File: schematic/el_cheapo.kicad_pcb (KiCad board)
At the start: 2 copper layers, 100.7 x 80.4 mm, 57 parts, among them J1 Conn_01x02, J2 Conn_01x02, J3 Conn_01x02, Q1 TIP32A, Q2 2N3904, Q3 2N3906, Q4 2N3904, Q5 TIP31A, Q6 TIP32A, Q7 2N3055, Q8 2N3055

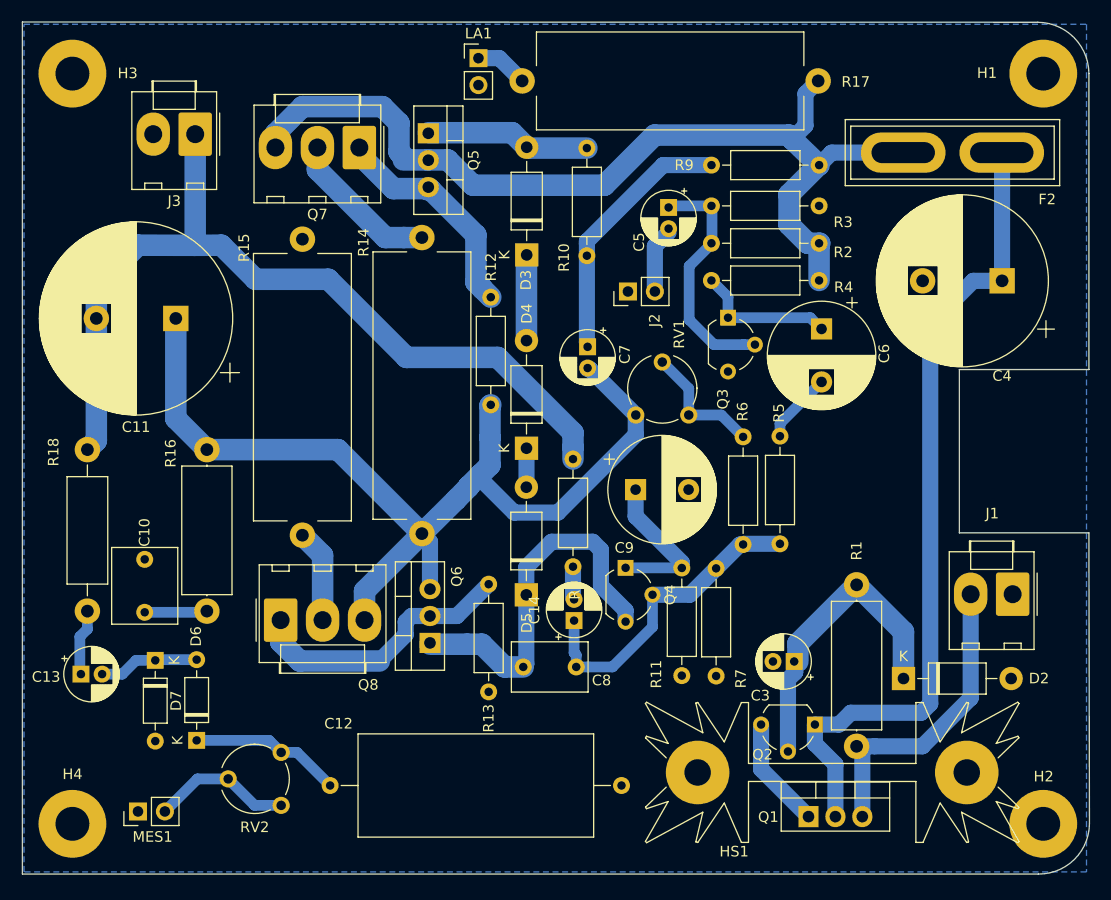
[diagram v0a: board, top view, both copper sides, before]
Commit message: first decent version of dual channel opamp version.
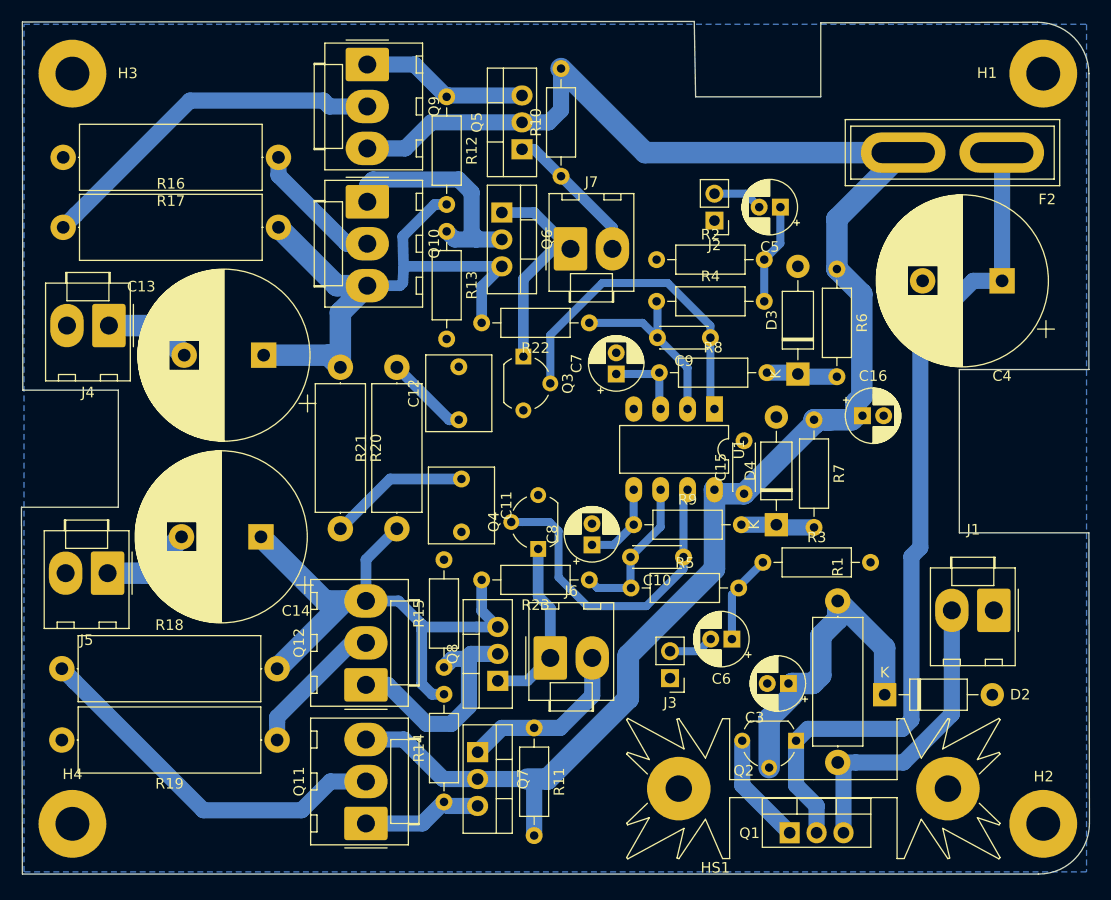
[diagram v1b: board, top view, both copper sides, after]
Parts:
- removed D5: 1N4001, Diode_THT:D_DO-41_SOD81_P10.16mm_Horizontal
- removed D6, D7: 1N914, Diode_THT:D_DO-35_SOD27_P7.62mm_Horizontal
- removed LA1: Lamp, Connector_PinHeader_2.54mm:PinHeader_1x02_P2.54mm_Vertical
- removed MES1: Amperemeter_DC, Connector_PinHeader_2.54mm:PinHeader_1x02_P2.54mm_Vertical
- removed RV1: 120k, Potentiometer_THT:Potentiometer_Piher_PT-6-V_Vertical
- removed RV2: 1k_100K, Potentiometer_THT:Potentiometer_Piher_PT-6-V_Vertical
- added C15: 0.1uF, Capacitor_THT:C_Disc_D4.3mm_W1.9mm_P5.00mm, F.Cu at (155.7, 102.6)
- added C16: 10uF, Capacitor_THT:CP_Radial_D5.0mm_P2.00mm, F.Cu at (166.9, 95.2)
- added J4: Conn_01x02, Connector_Molex:Molex_KK-396_A-41791-0002_1x02_P3.96mm_Vertical, F.Cu at (95.8, 86.7)
- added J5: Conn_01x02, Connector_Molex:Molex_KK-396_A-41791-0002_1x02_P3.96mm_Vertical, F.Cu at (95.6, 110.1)
- added J6: Conn_01x02, Connector_Molex:Molex_KK-396_A-41791-0002_1x02_P3.96mm_Vertical, F.Cu at (137.4, 118.1)
- added J7: Conn_01x02, Connector_Molex:Molex_KK-396_A-41791-0002_1x02_P3.96mm_Vertical, F.Cu at (139.3, 79.5)
- added Q10: 2N3055, Connector_Molex:Molex_KK-396_A-41791-0003_1x03_P3.96mm_Vertical, F.Cu at (120.1, 75.1)
- added Q11: 2N3055, Connector_Molex:Molex_KK-396_A-41791-0003_1x03_P3.96mm_Vertical, F.Cu at (120.0, 133.7)
- added Q12: 2N3055, Connector_Molex:Molex_KK-396_A-41791-0003_1x03_P3.96mm_Vertical, F.Cu at (120.0, 120.7)
- added Q9: 2N3055, Connector_Molex:Molex_KK-396_A-41791-0003_1x03_P3.96mm_Vertical, F.Cu at (120.1, 62.1)
- added R19: 0R47 1W, Resistor_THT:R_Axial_DIN0617_L17.0mm_D6.0mm_P20.32mm_Horizontal, F.Cu at (111.6, 125.9)
- added R20: 18R 1W, Resistor_THT:R_Axial_DIN0414_L11.9mm_D4.5mm_P15.24mm_Horizontal, F.Cu at (117.6, 90.7)
- added R21: 18R 1W, Resistor_THT:R_Axial_DIN0414_L11.9mm_D4.5mm_P15.24mm_Horizontal, F.Cu at (122.9, 105.9)
- added R22: 100K, Resistor_THT:R_Axial_DIN0207_L6.3mm_D2.5mm_P10.16mm_Horizontal, F.Cu at (141.1, 86.5)
- added R23: 100K, Resistor_THT:R_Axial_DIN0207_L6.3mm_D2.5mm_P10.16mm_Horizontal, F.Cu at (141.1, 110.7)
- added U1: NE5532, Package_DIP:DIP-8_W7.62mm_LongPads, F.Cu at (152.9, 94.6)
- C10: value 100nF -> 22pF; footprint Capacitor_THT:C_Rect_L7.0mm_W6.0mm_P5.00mm -> Capacitor_THT:C_Disc_D4.3mm_W1.9mm_P5.00mm
- C11: value 2200uF -> 100nF; footprint Capacitor_THT:CP_Radial_D18.0mm_P7.50mm -> Capacitor_THT:C_Rect_L7.0mm_W6.0mm_P5.00mm
- C12: value 0.1uF -> 100nF; footprint Capacitor_THT:C_Axial_L22.0mm_D9.5mm_P27.50mm_Horizontal -> Capacitor_THT:C_Rect_L7.0mm_W6.0mm_P5.00mm
- C13: value 10uF -> 2200uF; footprint Capacitor_THT:CP_Radial_D5.0mm_P2.00mm -> Capacitor_THT:CP_Radial_D16.0mm_P7.50mm
- C14: value 47uF -> 2200uF; footprint Capacitor_THT:CP_Radial_D5.0mm_P2.00mm -> Capacitor_THT:CP_Radial_D16.0mm_P7.50mm
- C6: value 220uF -> 10uF; footprint Capacitor_THT:CP_Radial_D10.0mm_P5.00mm -> Capacitor_THT:CP_Radial_D5.0mm_P2.00mm
- C7: value 22uF -> 10uF
- C8: value 100pF -> 10uF; footprint Capacitor_THT:C_Rect_L7.0mm_W4.5mm_P5.00mm -> Capacitor_THT:CP_Radial_D5.0mm_P2.00mm
- C9: value 220uF -> 22pF; footprint Capacitor_THT:CP_Radial_D10.0mm_P5.00mm -> Capacitor_THT:C_Disc_D4.3mm_W1.9mm_P5.00mm
- D2: value 33 -> 39V
- D3, D4: value 1N4001 -> 1N47xxA
- F2: value 1A -> 2A
- J3: footprint Connector_Molex:Molex_KK-396_A-41791-0002_1x02_P3.96mm_Vertical -> Connector_PinHeader_2.54mm:PinHeader_1x02_P2.54mm_Vertical
- Q4: value 2N3904 -> 2N3906
- Q7: value 2N3055 -> TIP31A; footprint Connector_Molex:Molex_KK-396_A-41791-0003_1x03_P3.96mm_Vertical -> Package_TO_SOT_THT:TO-220-3_Vertical
- Q8: value 2N3055 -> TIP32A; footprint Connector_Molex:Molex_KK-396_A-41791-0003_1x03_P3.96mm_Vertical -> Package_TO_SOT_THT:TO-220-3_Vertical
- R10: value 3K3 -> 1k
- R11: value 330R -> 1K
- R14, R15: value 0R47 1W -> 270; footprint Resistor_THT:R_Axial_Power_L25.0mm_W9.0mm_P27.94mm -> Resistor_THT:R_Axial_DIN0207_L6.3mm_D2.5mm_P10.16mm_Horizontal
- R16: value 18R 1W -> 0R47 1W; footprint Resistor_THT:R_Axial_DIN0414_L11.9mm_D4.5mm_P15.24mm_Horizontal -> Resistor_THT:R_Axial_DIN0617_L17.0mm_D6.0mm_P20.32mm_Horizontal
- R17: value 470R 2W -> 0R47 1W; footprint Resistor_THT:R_Axial_Power_L25.0mm_W9.0mm_P27.94mm -> Resistor_THT:R_Axial_DIN0617_L17.0mm_D6.0mm_P20.32mm_Horizontal
- R18: value 1k_100k 1W -> 0R47 1W; footprint Resistor_THT:R_Axial_DIN0411_L9.9mm_D3.6mm_P15.24mm_Horizontal -> Resistor_THT:R_Axial_DIN0617_L17.0mm_D6.0mm_P20.32mm_Horizontal
- R2, R3: value 220k -> 100k
- R4: value 10k -> 12k
- R5: value 1k -> 12k
- R6: value 22k -> 22K
- R7: value 10K -> 22K
- R8: value 15K -> 100K
- R9: value 2K2 -> 100K
- moved J3 68.1 mm to (148.7, 120.0)
- moved Q7 58.1 mm to (130.6, 127.0), turned to 270 degrees
- moved R14 53.3 mm to (127.4, 131.7), turned to 90 degrees
- moved R17 51.4 mm to (111.8, 70.9)
- moved C10 51.1 mm to (150.0, 108.6), turned to 180 degrees
- moved Q6 41.2 mm to (132.8, 76.1), turned to 270 degrees
- moved C12 36.6 mm to (128.8, 95.6), turned to 90 degrees
- moved R9 34.7 mm to (145.3, 105.5)
- moved C13 34.7 mm to (110.4, 89.5), turned to 180 degrees
- moved R3 34.0 mm to (157.5, 109.1)
- moved R13 33.5 mm to (127.6, 77.9)
- moved C11 30.9 mm to (129.0, 101.2), turned to 270 degrees
- moved C14 30.6 mm to (110.1, 106.7), turned to 180 degrees
- moved C6 30.5 mm to (154.6, 116.3), turned to 180 degrees
- moved D3 28.0 mm to (160.8, 91.3)
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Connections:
- net /amp/AUDIO_IN renamed Net-(C5-Pad2)
- net /amp/N_EMITTER renamed Net-(Q12-Pad1)
- C10 pad 2: GND -> Net-(C10-Pad2)
- C11 pad 1: /amp/N_COLLECTOR -> Net-(C11-Pad1)
- C11 pad 2: /amp/AUDIO_OUT -> GND
- C7 pad 2: /amp/N_COLLECTOR -> GND
- C8 pad 2: Net-(C14-Pad1) -> GND
- C9 pad 2: GND -> Net-(C9-Pad2)
- D3 pad 2: Net-(D3-Pad2) -> GND
- D4 pad 2: Net-(D3-Pad1) -> GND
- J3 pad 1: /amp/AUDIO_OUT -> GND
- J3 pad 2: GND -> Net-(C6-Pad2)
- Q3 pad 1: Net-(C6-Pad1) -> Net-(D7-Pad1)
- Q3 pad 2: Net-(C5-Pad1) -> Net-(C9-Pad1)
- Q4 pad 1: Net-(C9-Pad1) -> Net-(D10-Pad1)
- Q4 pad 2: Net-(C14-Pad1) -> Net-(C10-Pad1)
- Q4 pad 3: Net-(C8-Pad1) -> GND
- Q5 pad 1: Net-(D3-Pad2) -> Net-(D5-Pad2)
- Q5 pad 3: /amp/P_BASE -> Net-(Q5-Pad3)
- Q6 pad 1: Net-(C8-Pad1) -> Net-(D7-Pad1)
- Q6 pad 2: /amp/N_BASE -> Net-(Q10-Pad1)
- Q6 pad 3: /amp/N_COLLECTOR -> Net-(C13-Pad1)
- Q7 pad 1: /amp/P_BASE -> Net-(D8-Pad2)
- Q7 pad 2: /amp/P_EMITTER -> /amp/+V
- Q7 pad 3: /amp/+V -> Net-(Q11-Pad1)
- Q8 pad 1: /amp/N_BASE -> Net-(D10-Pad1)
- Q8 pad 3: /amp/N_COLLECTOR -> Net-(C14-Pad1)
- R10 pad 1: Net-(C7-Pad1) -> Net-(D5-Pad2)
- R10 pad 2: Net-(D3-Pad2) -> /amp/+V
- R11 pad 1: Net-(C9-Pad1) -> Net-(D8-Pad2)
- R11 pad 2: GND -> /amp/+V
- R12 pad 1: /amp/P_BASE -> Net-(Q5-Pad3)
- R12 pad 2: /amp/N_COLLECTOR -> Net-(C13-Pad1)
- R13 pad 1: /amp/N_BASE -> Net-(Q10-Pad1)
- R14 pad 1: /amp/P_EMITTER -> Net-(Q11-Pad1)
- R14 pad 2: /amp/N_COLLECTOR -> Net-(C14-Pad1)
- R16 pad 1: /amp/N_COLLECTOR -> Net-(Q9-Pad2)
- R16 pad 2: Net-(C10-Pad1) -> Net-(C13-Pad1)
- R17 pad 1: /amp/+V -> Net-(Q10-Pad2)
- R17 pad 2: Net-(LA1-Pad1) -> GND
- R18 pad 1: /amp/AUDIO_OUT -> Net-(Q11-Pad2)
- R18 pad 2: Net-(C13-Pad1) -> Net-(C14-Pad1)
- R2 pad 1: /amp/+V -> GND
- R3 pad 1: Net-(C5-Pad1) -> Net-(C6-Pad1)
- R4 pad 1: /amp/+V -> Net-(C9-Pad2)
- R4 pad 2: Net-(C6-Pad1) -> Net-(C5-Pad1)
- R5 pad 1: Net-(C14-Pad1) -> Net-(C10-Pad2)
- R5 pad 2: Net-(C6-Pad2) -> Net-(C6-Pad1)
- R6 pad 1: Net-(R6-Pad1) -> /amp/+V
- R6 pad 2: Net-(C14-Pad1) -> Net-(D3-Pad1)
- R7 pad 1: Net-(C14-Pad1) -> /amp/+V
- R7 pad 2: GND -> Net-(D4-Pad1)
- R8 pad 1: /amp/AUDIO_OUT -> Net-(C7-Pad1)
- R8 pad 2: Net-(C14-Pad2) -> Net-(D3-Pad1)
- R9 pad 1: Net-(C7-Pad1) -> Net-(C8-Pad1)
- R9 pad 2: /amp/+V -> Net-(D4-Pad1)
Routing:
- net /amp/N_COLLECTOR: track 95.6 -> 0.00 mm
- net /amp/AUDIO_OUT: track 82.6 -> 0.00 mm
- net /amp/+V: track 90.4 -> 167.3 mm
- net Net-(C13-Pad1): track 6.24 -> 56.2 mm
- net Net-(Q11-Pad2): track 0.00 -> 36.7 mm
- net Net-(Q9-Pad2): track 0.00 -> 33.9 mm
- net Net-(C8-Pad1): track 36.2 -> 8.03 mm
- net Net-(C14-Pad1): track 30.4 -> 58.2 mm
- net /amp/N_BASE: track 26.2 -> 0.00 mm
- net Net-(C10-Pad1): track 5.91 -> 31.2 mm
- net Net-(Q10-Pad1): track 0.00 -> 22.3 mm
- net Net-(D7-Pad1): track 0.00 -> 21.7 mm
- net /amp/P_BASE: track 21.4 -> 0.00 mm
- net Net-(D8-Pad2): track 0.00 -> 19.1 mm
- net Net-(C9-Pad2): track 0.00 -> 18.4 mm
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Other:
- board size 100.7 x 80.4 mm -> 100.8 x 80.5 mm
- net class opamp added: clearance 0.5334, trace_width 0.762, via_dia 0.8, via_drill 0.4

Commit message: cleanup and remove resistor
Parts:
- removed R2, R3: 100k, Resistor_THT:R_Axial_DIN0207_L6.3mm_D2.5mm_P10.16mm_Horizontal
- added D11: 1N4001, Diode_THT:D_DO-41_SOD81_P10.16mm_Horizontal, F.Cu at (161.7, 80.6)
- added D12: 1N4001, Diode_THT:D_DO-41_SOD81_P10.16mm_Horizontal, F.Cu at (161.8, 98.9)
- added D13: 1N4001, Diode_THT:D_DO-41_SOD81_P10.16mm_Horizontal, F.Cu at (158.5, 90.8)
- added D14: 1N4001, Diode_THT:D_DO-41_SOD81_P10.16mm_Horizontal, F.Cu at (158.5, 109.1)
- C10, C9: value 22pF -> 1pF
- R22, R23: value 100K -> 470k
- R4, R5: value 12k -> 47k
- moved C5 8.15 mm to (151.0, 76.2), turned to 0 degrees
- moved D4 7.50 mm to (165.4, 109.1)
- moved J2 7.31 mm to (160.1, 75.8), turned to 270 degrees
- moved R7 7.16 mm to (168.7, 98.9)
- moved C4 4.82 mm to (175.3, 82.0), turned to 0 degrees
- moved D3 4.36 mm to (165.1, 90.7)
- moved R6 3.99 mm to (168.4, 80.8)
- moved C7 2.56 mm to (141.4, 90.2), turned to 270 degrees
- moved R8 2.19 mm to (145.5, 90.8)
- moved C16 1.82 mm to (168.7, 94.9), turned to 180 degrees
- moved C9 1.14 mm to (151.4, 87.9)
- turned R4 to 90 degrees
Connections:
- D3 pad 2: GND -> Net-(D11-Pad1)
- D4 pad 2: GND -> Net-(D12-Pad1)
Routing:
- net Net-(D3-Pad1): track 6.76 -> 15.8 mm
- net Net-(D4-Pad1): track 6.96 -> 14.7 mm
- net Net-(C5-Pad1): track 9.52 -> 4.35 mm
- net Net-(D12-Pad1): track 0.00 -> 3.56 mm
- net Net-(D11-Pad1): track 0.00 -> 3.48 mm
- net Net-(D12-Pad2): track 0.00 -> 3.30 mm
- net Net-(C6-Pad1): track 8.45 -> 5.22 mm
- net Net-(D11-Pad2): track 0.00 -> 3.17 mm
- net /amp/+V: track 167.3 -> 170.2 mm
- net Net-(C7-Pad1): track 7.60 -> 9.21 mm
- net Net-(C4-Pad1): track 79.9 -> 81.0 mm
- net Net-(C9-Pad1): track 31.6 -> 32.3 mm
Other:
- outline, holes or cut-outs redrawn
